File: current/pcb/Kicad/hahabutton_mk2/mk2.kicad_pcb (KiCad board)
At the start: 2 copper layers, 138 parts, among them U1 SAMB11G18A, Y1 32.768kHz, Y2 26MHz

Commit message: taking form, mkii...
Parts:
- removed the REF** at (170.4, 97.3)
- removed the REF** at (139.9, 107.4)
- removed the REF** at (139.9, 112.5)
- removed the REF** at (139.9, 122.7)
- removed the REF** at (139.9, 117.6)
- removed the REF** at (134.8, 117.6)
- removed the REF** at (134.8, 122.7)
- removed the REF** at (67.2, 128.3)
- removed the REF** at (165.3, 97.3)
- removed the REF** at (165.3, 102.4)
- removed the REF** at (170.4, 102.4)
- removed the REF** at (166.6, 51.6)
- removed the REF** at (171.7, 56.6)
- removed the REF** at (129.7, 46.5)
- removed the REF** at (171.7, 51.6)
- removed the REF** at (166.6, 56.6)
- removed the REF** at (129.7, 41.4)
- removed the REF** at (151.3, 36.3)
- removed the REF** at (132.3, 75.7)
- removed the REF** at (130.4, 73.2)
- removed the REF** at (146.3, 36.3)
- removed the REF** at (175.5, 112.5)
- removed the REF** at (141.2, 41.4)
- removed the REF** at (141.2, 36.3)
- removed the REF** at (136.1, 41.4)
- removed the REF** at (136.1, 46.5)
- removed the REF** at (175.5, 117.6)
- removed the REF** at (170.4, 122.7)
- removed the REF** at (179.9, 66.8)
- removed the REF** at (179.9, 71.9)
- removed the REF** at (179.9, 61.7)
- removed the REF** at (170.4, 107.4)
- removed the REF** at (165.3, 122.7)
- removed the REF** at (165.3, 117.6)
- removed the REF** at (170.4, 117.6)
- removed the REF** at (160.2, 117.6)
- removed the REF** at (175.5, 107.4)
- removed the REF** at (160.2, 122.7)
- removed the REF** at (129.7, 122.7)
- removed the REF** at (129.7, 117.6)
- removed the REF** at (129.7, 107.4)
- removed the REF** at (175.5, 102.4)
- removed the REF** at (129.7, 112.5)
- removed the REF** at (129.7, 97.3)
- removed the REF** at (129.7, 92.2)
- removed the REF** at (129.7, 102.4)
- removed the REF** at (129.7, 87.1)
- removed the REF** at (129.7, 82.0)
- removed the REF** at (134.8, 82.0)
- removed the REF** at (134.8, 87.1)
- removed the REF** at (139.9, 87.1)
- removed the REF** at (134.8, 102.4)
- removed the REF** at (175.5, 97.3)
- removed the REF** at (139.9, 102.4)
- removed the REF** at (139.9, 97.3)
- removed the REF** at (139.9, 92.2)
- removed the REF** at (134.8, 92.2)
- removed the REF** at (134.8, 97.3)
- removed the REF** at (145.0, 97.3)
- removed the REF** at (145.0, 92.2)
- removed the REF** at (150.1, 97.3)
- removed the REF** at (150.1, 102.4)
- removed the REF** at (145.0, 102.4)
- removed the REF** at (160.2, 97.3)
- removed the REF** at (145.0, 122.7)
- removed the REF** at (145.0, 117.6)
- removed the REF** at (150.1, 117.6)
- removed the REF** at (150.1, 122.7)
- removed the REF** at (150.1, 112.5)
- removed the REF** at (150.1, 107.4)
- removed the REF** at (145.0, 107.4)
- removed the REF** at (145.0, 112.5)
- removed the REF** at (134.8, 112.5)
- removed the REF** at (134.8, 107.4)
- added BT1: Battery_Cell, Batteries:batt_holder3035, B.Cu at (130.7, 58.8)
- added D1: LED, LEDs:LED_0402_1005Metric, F.Cu at (203.0, 44.5)
- added D2: D_Schottky, Diodes:D_0402_1005Metric, F.Cu at (201.9, 37.8)
- C14, C16, C17, C19, L4: moved to F.Cu
- moved R2 142.8 mm to (203.0, 44.5)
- moved R3 132.7 mm to (203.0, 44.5), turned to 0 degrees
- moved C19 130.3 mm to (203.0, 44.5), turned to 0 degrees
- moved H1 94.7 mm to (158.9, 51.4), turned to 0 degrees
- moved C17 76.6 mm to (201.9, 37.8), turned to 0 degrees
- moved C16 76.2 mm to (201.9, 37.8), turned to 0 degrees
- moved L3 75.9 mm to (201.9, 37.8)
- moved C14 75.1 mm to (201.9, 37.8), turned to 0 degrees
- moved L4 74.6 mm to (201.9, 37.8), turned to 0 degrees
- moved C21 51.5 mm to (124.3, 89.3)
- moved C22 51.5 mm to (124.3, 88.4)
- moved C23 51.5 mm to (124.3, 87.5)
- moved REF** 51.5 mm to (121.4, 81.5)
- moved R4 51.5 mm to (126.8, 82.6)
- moved R5 51.5 mm to (119.4, 84.5)
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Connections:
- AE1 pad 1: /SIG_2.4G -> GND
- C7 pad 1: /SIG_2.4G -> GND
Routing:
- net /+3.3V: track 206.2 -> 1.77 mm, vias 3 -> 0
- net /RESET: track 102.3 -> 0.00 mm, vias 4 -> 0
- net /SWO: track 93.8 -> 0.00 mm
- net Net-(U1-Pad9): track 81.3 -> 0.00 mm, vias 1 -> 0
- net /SWDCLK: track 80.3 -> 0.01 mm
- net /SWDIO: track 80.0 -> 0.00 mm
- net Net-(U1-Pad11): track 79.0 -> 0.00 mm, vias 1 -> 0
- net /+3.0V: track 78.1 -> 1.45 mm, vias 10 -> 1
- net /LED_WARN: track 75.0 -> 0.00 mm
- net Net-(U1-Pad16): track 66.3 -> 0.00 mm
- net /+5V: track 66.4 -> 0.90 mm
- net Net-(U1-Pad8): track 64.7 -> 0.00 mm, vias 1 -> 0
- net Net-(U1-Pad10): track 64.2 -> 0.00 mm, vias 1 -> 0
- net Net-(U1-Pad17): track 63.3 -> 0.00 mm, vias 1 -> 0
- net Net-(U1-Pad14): track 62.9 -> 0.00 mm
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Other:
- board text removed: "C"
- board text removed: "Light"

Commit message: not much change...
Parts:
- removed C1: CP, Capacitors_SMD:C_0805
- removed C10, C19, C20, C22: 1.0uF, Capacitors_SMD:C_0402
- removed C11, C12, C13: 0.1uF, Capacitors_SMD:C_0402
- removed C14: 4.7uF 6.3V, Capacitors_SMD:C_0402
- removed C16: 2.2uF 6.3V, Capacitors_SMD:C_0402
- removed C17: 0.01uF, Capacitors_SMD:C_0402
- removed C21: 47pF, Capacitors_SMD:C_0402
- removed C23: 10uF, Capacitors_SMD:C_0402
- removed D1: LED, LEDs:LED_0402_1005Metric
- removed D2: D_Schottky, Diodes:D_0402_1005Metric
- removed FB1: BLM03AG121SN1, Capacitors_SMD:C_0603_HandSoldering
- removed L3: 9.1nH, Capacitors_SMD:C_0402
- removed L4: 4.7uH, Capacitors_SMD:C_0805_HandSoldering
- removed R2, R5: 1k, Capacitors_SMD:C_0402
- removed R3: 100k, Capacitors_SMD:C_0402
- removed R4: 100, Capacitors_SMD:C_0402
- removed the REF** at (161.5, 51.6)
- removed the REF** at (161.5, 56.6)
- removed the REF** at (147.5, 68.3)
- removed the REF** at (157.7, 68.3)
- removed the REF** at (151.3, 56.6)
- removed the REF** at (151.3, 46.5)
- removed the REF** at (161.5, 46.5)
- removed the REF** at (156.4, 46.5)
- removed the REF** at (156.4, 51.6)
- removed the REF** at (151.3, 51.6)
- removed the REF** at (128.4, 74.9)
- removed the REF** at (128.4, 80.0)
- removed the REF** at (116.4, 76.4)
- removed the REF** at (121.4, 81.5)
- removed the REF** at (162.8, 73.4)
- removed the REF** at (152.6, 68.3)
- removed the REF** at (166.6, 46.5)
- removed the REF** at (146.3, 46.5)
- removed the REF** at (156.4, 56.6)
- removed R_LED1: R, Capacitors_SMD:C_0402
- moved H1 55.6 mm to (127.2, 97.1), turned to 270 degrees
- moved B1 4.24 mm to (139.6, 62.6)
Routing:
- net Net-(C10-Pad1): track 11.4 -> 0.22 mm, vias 3 -> 0
- net Net-(C13-Pad1): track 3.46 -> 0.00 mm, vias 2 -> 0
- net /+3.3V: track 1.77 -> 0.00 mm
- net /+5V: track 0.90 -> 0.00 mm
- net /+3.0V: track 1.45 -> 0.89 mm, vias 1 -> 0
- net GND: track 0.00 -> 0.56 mm, vias 0 -> 1
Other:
- board text removed: "+3.3V"
- board text removed: "+5V"
- board text removed: "1"
- board text removed: "AUDIO"
- board text removed: "B"
- board text removed: "GND"

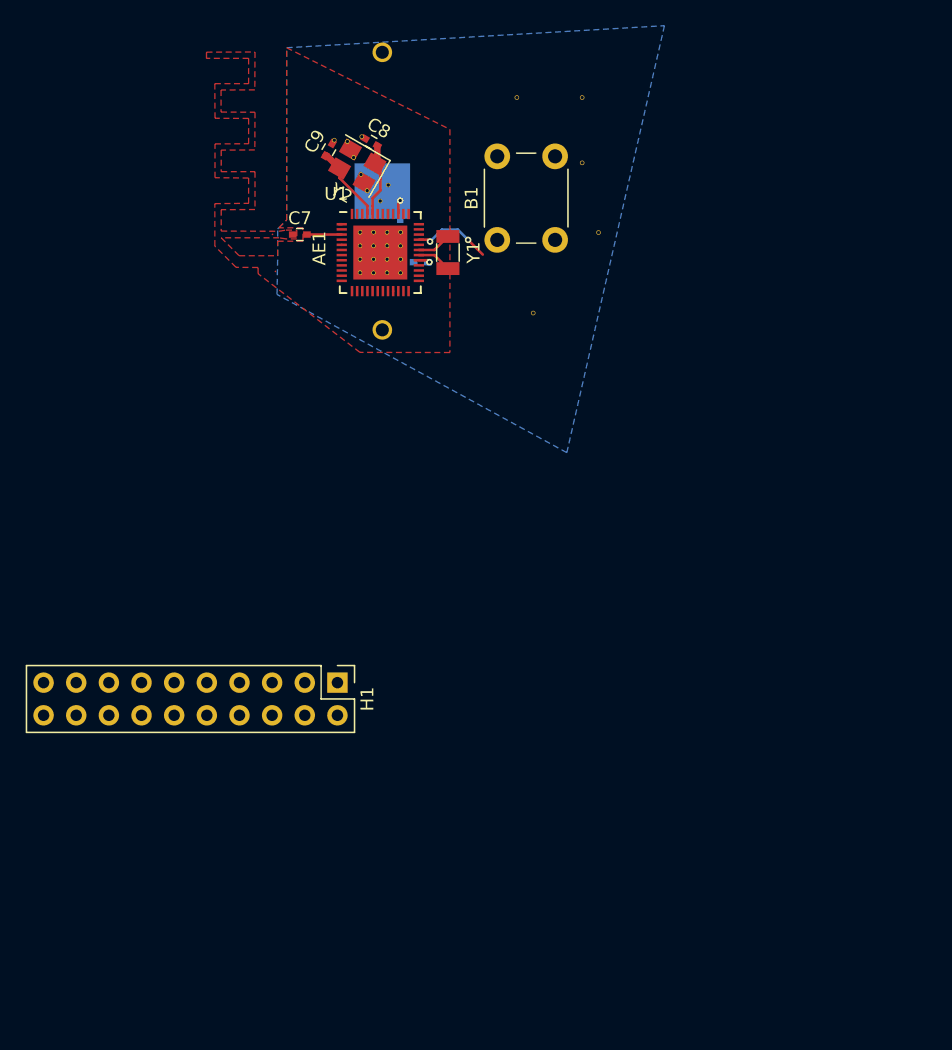
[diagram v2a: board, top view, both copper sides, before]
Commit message: fixed footprint paths; the progression to 2.0 continues...
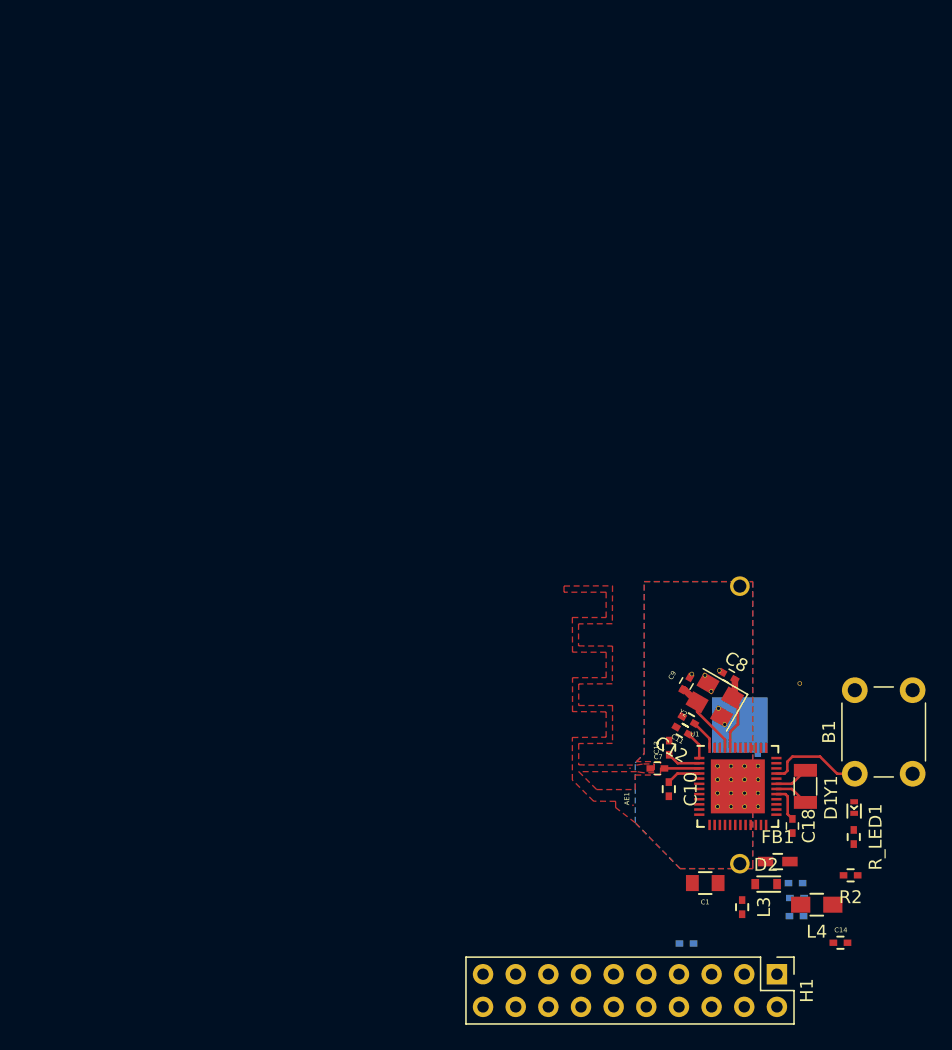
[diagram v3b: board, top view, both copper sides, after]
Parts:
- removed the REF** at (147.5, 62.1)
- removed the REF** at (142.4, 68.3)
- removed the REF** at (141.2, 51.6)
- removed the REF** at (146.3, 51.6)
- removed the REF** at (146.3, 56.6)
- removed the REF** at (130.5, 59.6)
- added C1: CP, Capacitors_SMD:C_0805, F.Cu at (155.8, 112.7)
- added C10: 1.0uF, Capacitors_SMD:C_0402, F.Cu at (153.0, 105.4)
- added C11: 0.1uF, Capacitors_SMD:C_0402, F.Cu at (154.5, 100.0)
- added C12: 0.1uF, Capacitors_SMD:C_0402, F.Cu at (154.0, 100.8)
- added C13: 0.1uF, Capacitors_SMD:C_0402, F.Cu at (153.0, 102.1)
- added C14: 4.7uF 6.3V, Capacitors_SMD:C_0402, F.Cu at (166.3, 117.3)
- added C16: 2.2uF 6.3V, Capacitors_SMD:C_0402, B.Cu at (162.9, 112.7)
- added C17: 0.01uF, Capacitors_SMD:C_0402, B.Cu at (163.0, 113.8)
- added C19: 1.0uF, Capacitors_SMD:C_0402, B.Cu at (162.9, 115.2)
- added D1: LED, LEDs:LED_0402, F.Cu at (167.4, 106.8)
- added D2: D_Schottky, Diodes_SMD:D_0603, F.Cu at (160.6, 112.8)
- added FB1: BLM03AG121SN1, Capacitors_SMD:C_0603_HandSoldering, F.Cu at (161.5, 111.0)
- added L3: 9.1nH, Capacitors_SMD:C_0402, F.Cu at (158.7, 114.5)
- added L4: 4.7uH, Capacitors_SMD:C_0805_HandSoldering, F.Cu at (164.5, 114.4)
- added R2: 1k, Capacitors_SMD:C_0402, F.Cu at (167.1, 112.1)
- added R3: 100k, Capacitors_SMD:C_0402, B.Cu at (154.4, 117.4)
- added R_LED1: R, Capacitors_SMD:C_0402, F.Cu at (167.4, 109.1)
- C18: moved to F.Cu
- moved C18 52.5 mm to (162.6, 108.2), turned to 270 degrees
- moved REF** 50.3 mm to (163.2, 97.1)
- moved C8 50.0 mm to (157.7, 96.6)
- moved REF** 50.0 mm to (156.9, 99.1)
- moved U1 50.0 mm to (158.4, 105.1)
- moved Y1 50.0 mm to (163.6, 105.1)
- moved C9 50.0 mm to (154.4, 97.1)
- moved REF** 50.0 mm to (156.3, 97.8)
- moved B1 50.0 mm to (167.5, 104.2)
- moved C15 50.0 mm to (159.9, 102.0)
- moved C7 50.0 mm to (152.1, 103.7)
- moved REF** 50.0 mm to (154.8, 96.4)
- moved REF** 50.0 mm to (155.8, 96.5)
- moved Y2 50.0 mm to (156.6, 98.4)
- moved AE1 50.0 mm to (146.4, 98.0)
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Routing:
- net Net-(C10-Pad1): track 0.22 -> 7.45 mm
- net Net-(C13-Pad1): track 0.00 -> 2.62 mm
- net Net-(C18-Pad1): track 1.01 -> 2.86 mm, vias 1 -> 0
- net /BTN_HELP: track 6.22 -> 7.61 mm, vias 2 -> 0
- net /+3.0V: track 0.89 -> 0.00 mm
- net GND: track 0.56 -> 0.35 mm, vias 1 -> 0
